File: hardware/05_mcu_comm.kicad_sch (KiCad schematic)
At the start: 0 parts

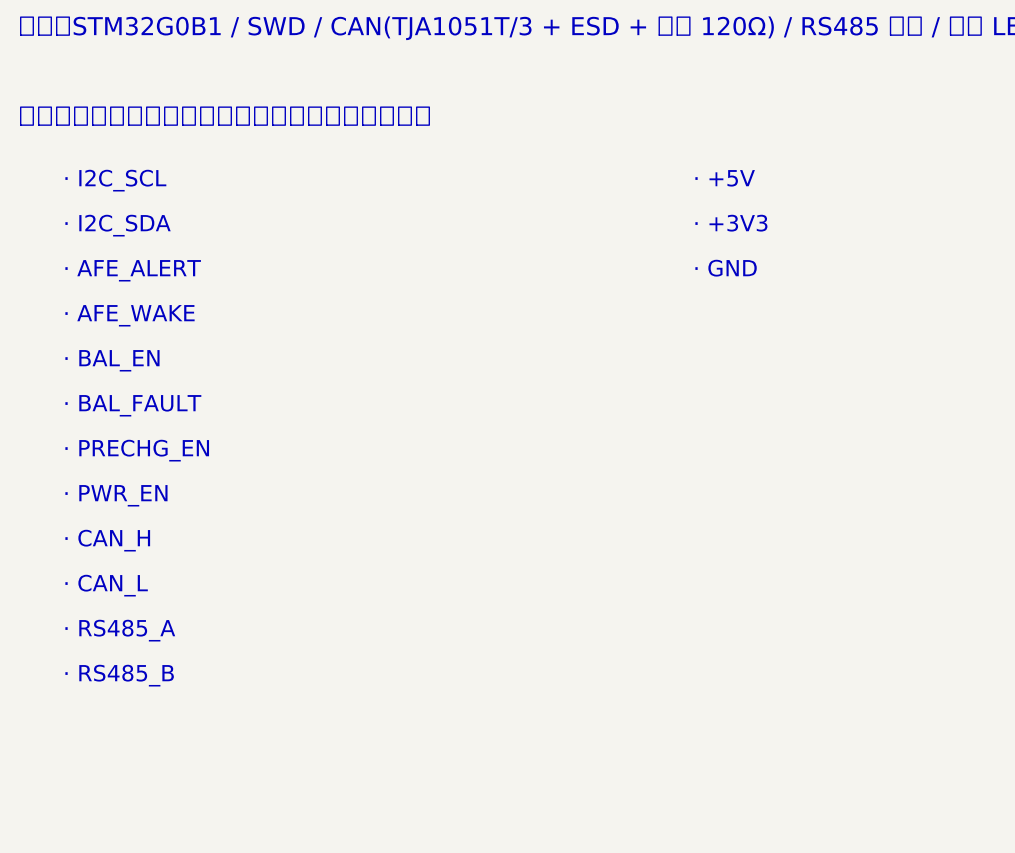
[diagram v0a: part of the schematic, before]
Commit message: v0.3：主动均衡改为 MP2643 ×7（MPS 客供），光耦跨电位控制，逐对均衡策略，BOM 与成本估算
- docs/03：均衡章节按 MP2643 手册 Rev1.1 重写（外围逐件点名、电流/限压计算、光耦接口、线束与发热）
- firmware：7 对 EN/MODE 输出，边界电荷盈亏定方向，相邻不同时开，收敛仿真测试
- tools/bms_calc.py：MP2643 手册公式；tools/jlc_api.py：嘉立创料号接口；tools/cost.py：成本估算
- docs/02-BOM.csv v0.3（81 行，带立创编号与来源），docs/05-成本估算.md
- KiCad 骨架更新（03 子图接口、网络类）

Co-Authored-By: Claude Opus 5.5 <noreply@anthropic.com>
Claude-Session: https://claude.ai/code/session_01EyFjq1nqLUmfVYESj2uYXd
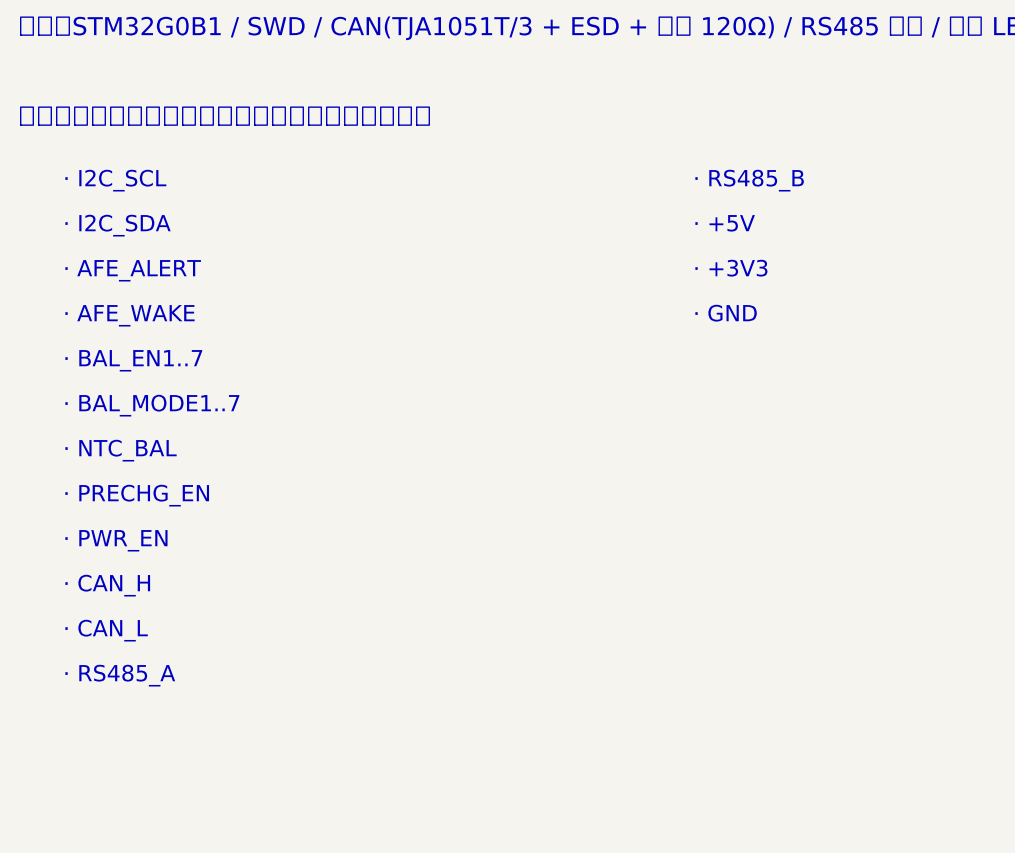
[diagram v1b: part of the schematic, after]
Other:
- note added: "· BAL_EN1..7"
- note added: "· BAL_MODE1..7"
- note added: "· NTC_BAL"
- note removed: "· BAL_EN"
- note removed: "· BAL_FAULT"
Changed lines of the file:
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@@
 		(title "MCU 与通讯")
 		(date "2026-09-26")
-		(rev "v0.2-skeleton")
+		(rev "v0.3-skeleton")
 		(company "MP2645A-BMS")
-		(comment 1 "8S LiFePO4 200A BMS · MPS MP2797 + MP2645A")
+		(comment 1 "8S LiFePO4 200A BMS · MPS MP2797 + MP2643x7")
 	)
 	(text "MCU 与通讯"
@@
 		)
 	)
-	(text "· BAL_EN"
+	(text "· BAL_EN1..7"
 		(exclude_from_sim no)
 		(at 25 72 0)
@@
 		)
 	)
-	(text "· BAL_FAULT"
+	(text "· BAL_MODE1..7"
 		(exclude_from_sim no)
 		(at 25 77 0)
@@
 		)
 	)
-	(text "· PRECHG_EN"
+	(text "· NTC_BAL"
 		(exclude_from_sim no)
 		(at 25 82 0)
@@
 		)
 	)
-	(text "· PWR_EN"
+	(text "· PRECHG_EN"
 		(exclude_from_sim no)
 		(at 25 87 0)
@@
 		)
 	)
-	(text "· CAN_H"
+	(text "· PWR_EN"
 		(exclude_from_sim no)
 		(at 25 92 0)
@@
 		)
 	)
-	(text "· CAN_L"
+	(text "· CAN_H"
 		(exclude_from_sim no)
 		(at 25 97 0)
@@
 		)
 	)
-	(text "· RS485_A"
+	(text "· CAN_L"
 		(exclude_from_sim no)
 		(at 25 102 0)
@@
 		)
 	)
-	(text "· RS485_B"
+	(text "· RS485_A"
 		(exclude_from_sim no)
 		(at 25 107 0)
@@
 		)
 	)
-	(text "· +5V"
+	(text "· RS485_B"
 		(exclude_from_sim no)
 		(at 95 52 0)
@@
 		)
 	)
-	(text "· +3V3"
+	(text "· +5V"
 		(exclude_from_sim no)
 		(at 95 57 0)
@@
 		)
 	)
-	(text "· GND"
+	(text "· +3V3"
 		(exclude_from_sim no)
 		(at 95 62 0)
 		(effects
 			(font
+				(size 1.8 1.8)
+			)
+			(justify left top)
+		)
+	)
+	(text "· GND"
+		(exclude_from_sim no)
+		(at 95 67 0)
+		(effects
+			(font

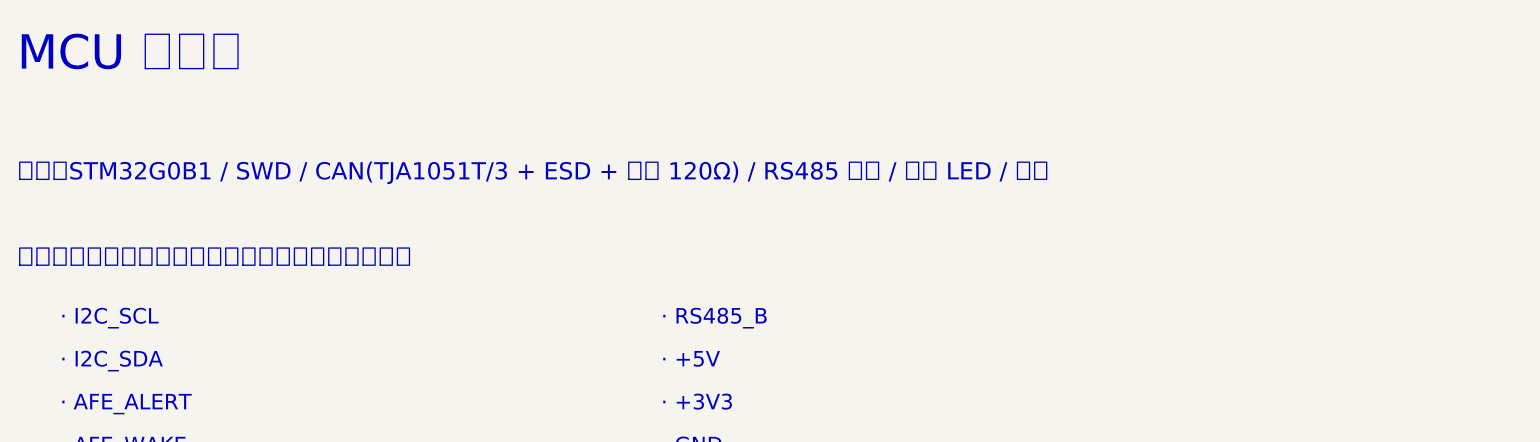
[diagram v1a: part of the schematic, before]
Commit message: v0.3 降本落地：Tokmas MOSFET×12、CH32V203、风华 4.7µF/100V、基础库阻值；MP2643 用 MPS 原厂 KiCad 库
- BOM：12 颗 Tokmas IPT012N08N5（C19626224）、CH32V203C8T6（C3001172）、C381466，MP2643 周边阻值改 0603 基础库等
- hardware/lib/mps：用户提供的 MP2643 符号/封装（已核对手册 p22 与引脚定义），注册到工程库表
- 计算器默认改为每方向 6 颗、Qg 240nC；测试按 Tj,max 150°C 留 30°C 裕量
- 成本：10 块 ¥587→¥393/块，100 块 ¥460→¥294/块（元器件）

Co-Authored-By: Claude Opus 5.5 <noreply@anthropic.com>
Claude-Session: https://claude.ai/code/session_01EyFjq1nqLUmfVYESj2uYXd
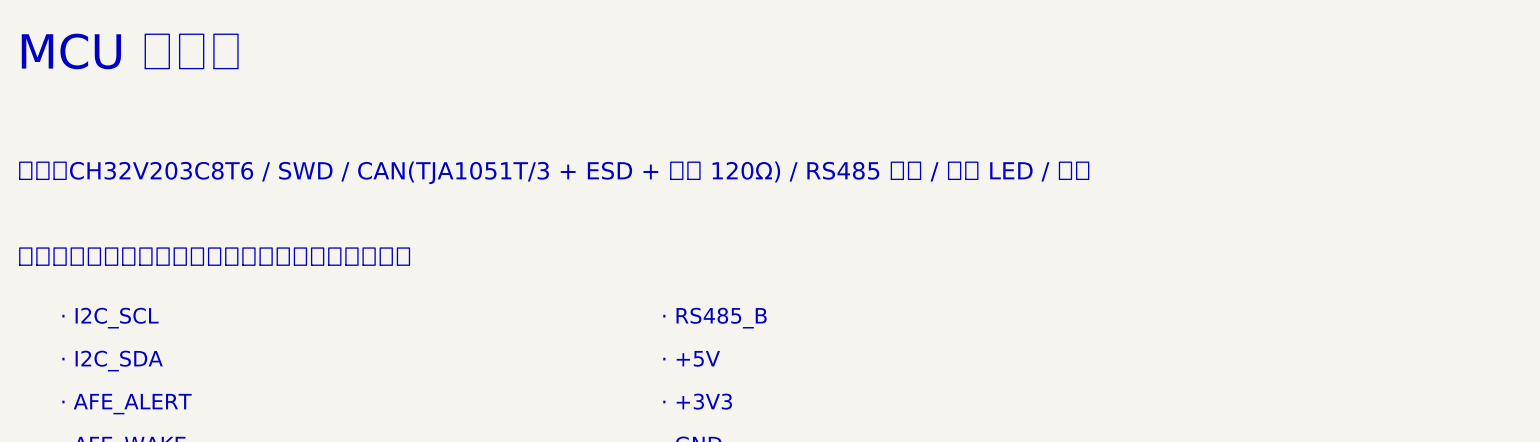
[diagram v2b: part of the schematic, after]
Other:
- note added: "内容：CH32V203C8T6 / SWD / CAN(TJA1051T/3 + ESD + 可选 120Ω) / RS485 可选 / 状态 LED / 按键"
- note removed: "内容：STM32G0B1 / SWD / CAN(TJA1051T/3 + ESD + 可选 120Ω) / RS485 可选 / 状态 LED / 按键"
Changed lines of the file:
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@@
 		)
 	)
-	(text "内容：STM32G0B1 / SWD / CAN(TJA1051T/3 + ESD + 可选 120Ω) / RS485 可选 / 状态 LED / 按键"
+	(text "内容：CH32V203C8T6 / SWD / CAN(TJA1051T/3 + ESD + 可选 120Ω) / RS485 可选 / 状态 LED / 按键"
 		(exclude_from_sim no)
 		(at 20 35 0)

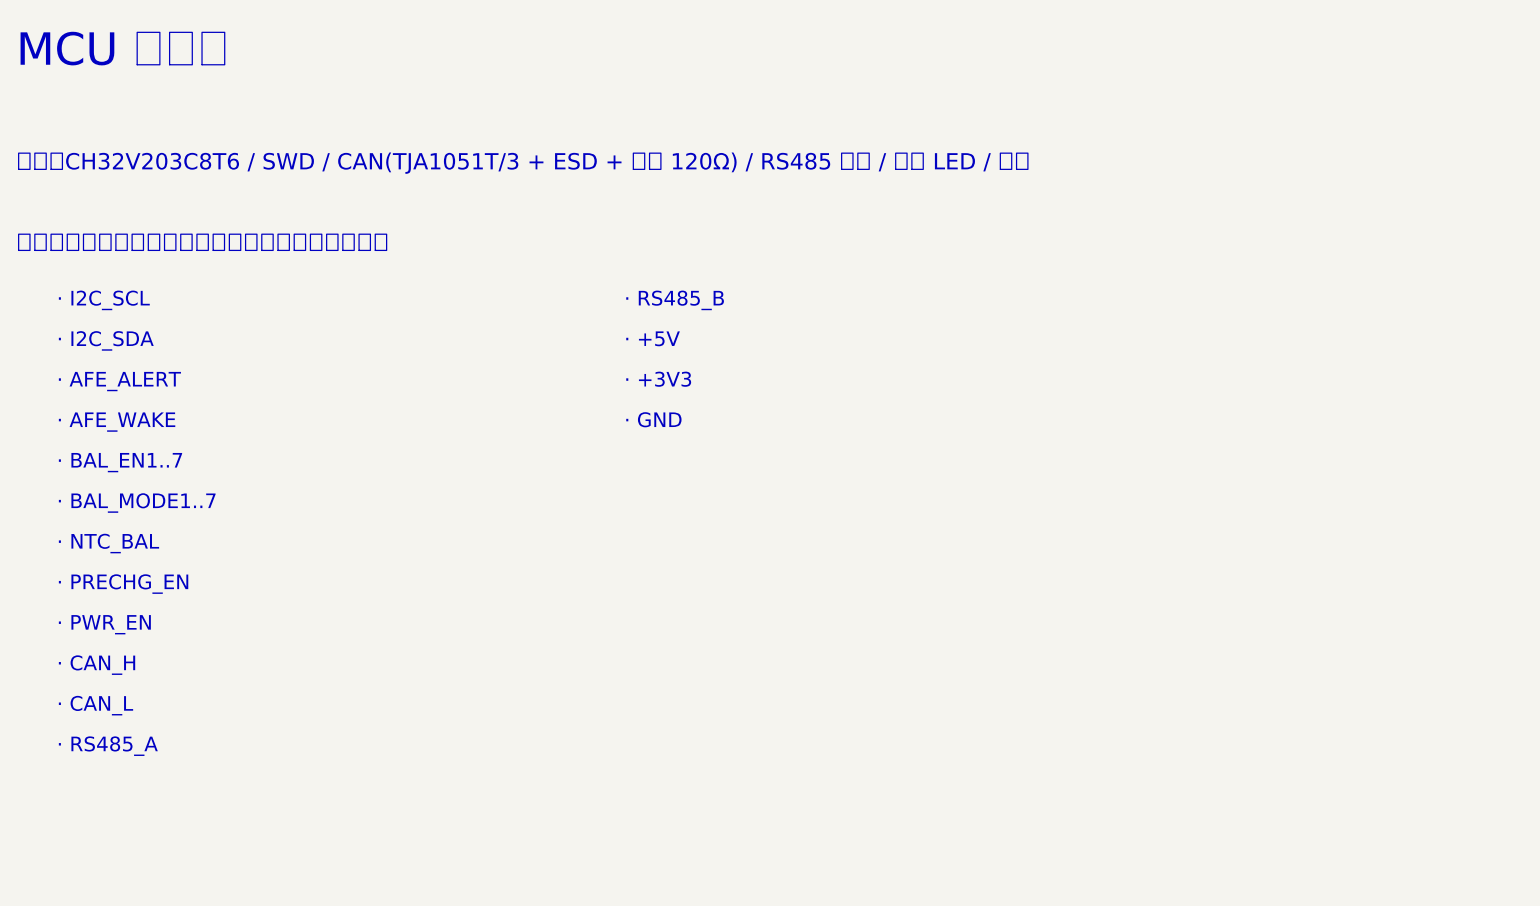
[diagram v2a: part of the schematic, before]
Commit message: 电源改为 LMR16006X 直降 3.3V + SN65HVD230（取消 5V 轨与 LDO）；会话交接文档与技能转移包
- BOM/详细设计/骨架：MP9486A+MP2013A+TJA1051 → LMR16006XDDCR(C87080)+SS210(C14996)+SN65HVD230DR(C12084)
- 成本（元器件）：10 块 ¥393→¥359/块，100 块 ¥294→¥267/块
- docs/00-会话交接.md：新会话的环境恢复、技能恢复、DeepSeek 画图方配置与待办
- transfer/pcb-workflow-skill.tar.gz：云主机上改写的 pcb-workflow 技能（仅用于转移）

Co-Authored-By: Claude Opus 5.5 <noreply@anthropic.com>
Claude-Session: https://claude.ai/code/session_01EyFjq1nqLUmfVYESj2uYXd
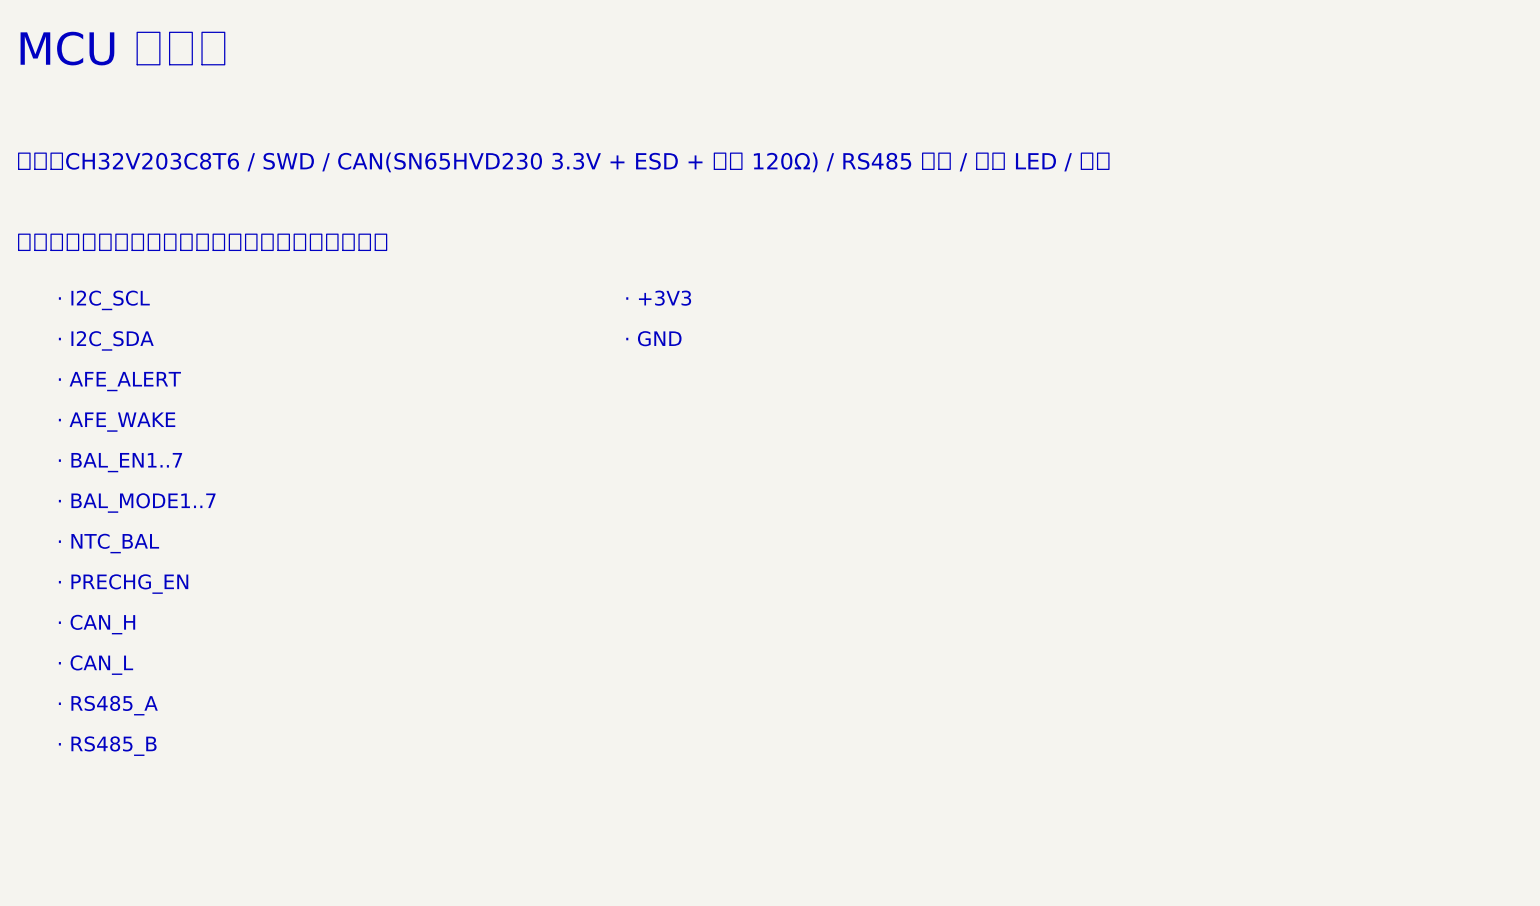
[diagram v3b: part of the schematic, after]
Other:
- note added: "内容：CH32V203C8T6 / SWD / CAN(SN65HVD230 3.3V + ESD + 可选 120Ω) / RS485 可选 / 状态 LED / 按键"
- note removed: "· +5V"
- note removed: "· PWR_EN"
- note removed: "内容：CH32V203C8T6 / SWD / CAN(TJA1051T/3 + ESD + 可选 120Ω) / RS485 可选 / 状态 LED / 按键"
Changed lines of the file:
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@@
 		)
 	)
-	(text "内容：CH32V203C8T6 / SWD / CAN(TJA1051T/3 + ESD + 可选 120Ω) / RS485 可选 / 状态 LED / 按键"
+	(text "内容：CH32V203C8T6 / SWD / CAN(SN65HVD230 3.3V + ESD + 可选 120Ω) / RS485 可选 / 状态 LED / 按键"
 		(exclude_from_sim no)
 		(at 20 35 0)
@@
 		)
 	)
-	(text "· PWR_EN"
+	(text "· CAN_H"
 		(exclude_from_sim no)
 		(at 25 92 0)
@@
 		)
 	)
-	(text "· CAN_H"
+	(text "· CAN_L"
 		(exclude_from_sim no)
 		(at 25 97 0)
@@
 		)
 	)
-	(text "· CAN_L"
+	(text "· RS485_A"
 		(exclude_from_sim no)
 		(at 25 102 0)
@@
 		)
 	)
-	(text "· RS485_A"
+	(text "· RS485_B"
 		(exclude_from_sim no)
 		(at 25 107 0)
@@
 		)
 	)
-	(text "· RS485_B"
+	(text "· +3V3"
 		(exclude_from_sim no)
 		(at 95 52 0)
@@
 		)
 	)
-	(text "· +5V"
+	(text "· GND"
 		(exclude_from_sim no)
 		(at 95 57 0)
 		(effects
 			(font
-				(size 1.8 1.8)
-			)
-			(justify left top)
-		)
-	)
-	(text "· +3V3"
-		(exclude_from_sim no)
-		(at 95 62 0)
-		(effects
-			(font
-				(size 1.8 1.8)
-			)
-			(justify left top)
-		)
-	)
-	(text "· GND"
-		(exclude_from_sim no)
-		(at 95 67 0)
-		(effects
-			(font

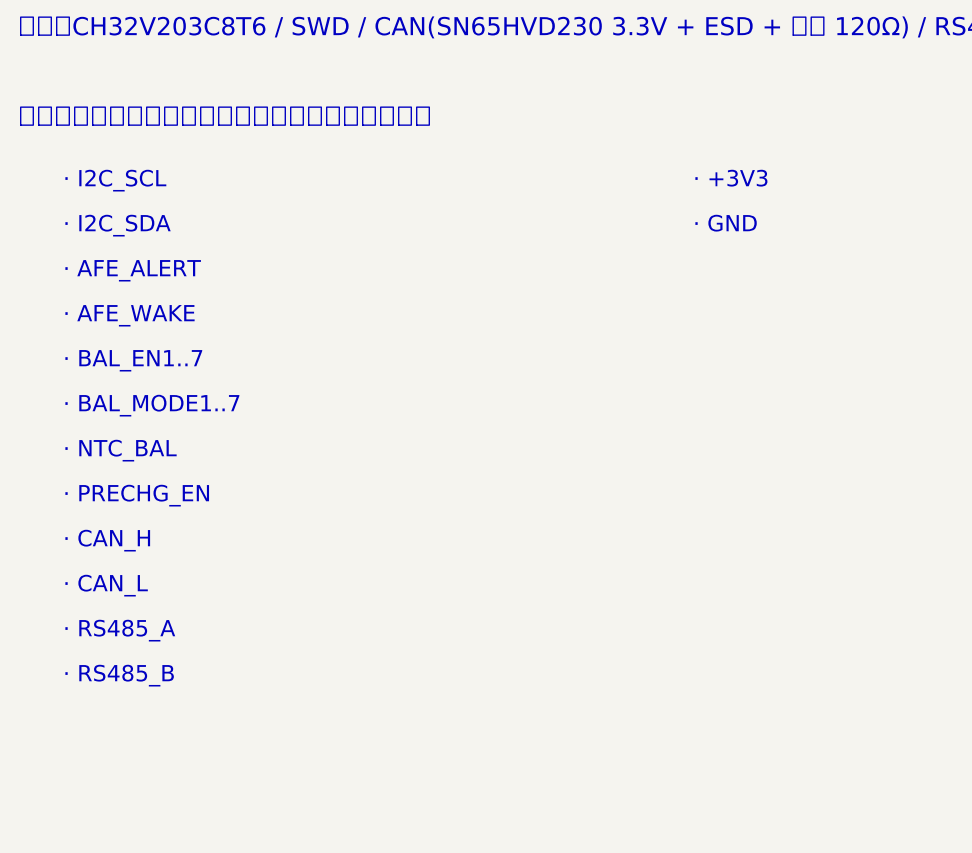
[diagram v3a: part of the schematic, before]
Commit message: 主动均衡改为分立开关电容（方案 B）：均衡部分约 ¥186→¥35/块
- 8 个互补半桥 AO3400A/AO3401A（基础库）+ 74LVC1G17 本节供电驱动，7 级飞电容 3×100µF，MCU BAL_CLK 50kHz 逐级电容耦合
- 固件：单一时钟使能；顶部/静置才开；压差>300mV 或任一节<3.0V 禁止；测试 37/37
- 计算器：sc_equalizer 模型（100mV≈0.21A，300mV≈0.62A）；测试 21/21
- BOM/成本：整板元器件 10 块 ¥359→¥202/块，100 块 ¥267→¥156/块
- 均衡端子改国产 2×5 Micro-Fit 兼容 C3030WV-2x5P（实测 3.0mm），节点保险丝 3A 1206

Co-Authored-By: Claude Opus 5.5 <noreply@anthropic.com>
Claude-Session: https://claude.ai/code/session_01EyFjq1nqLUmfVYESj2uYXd
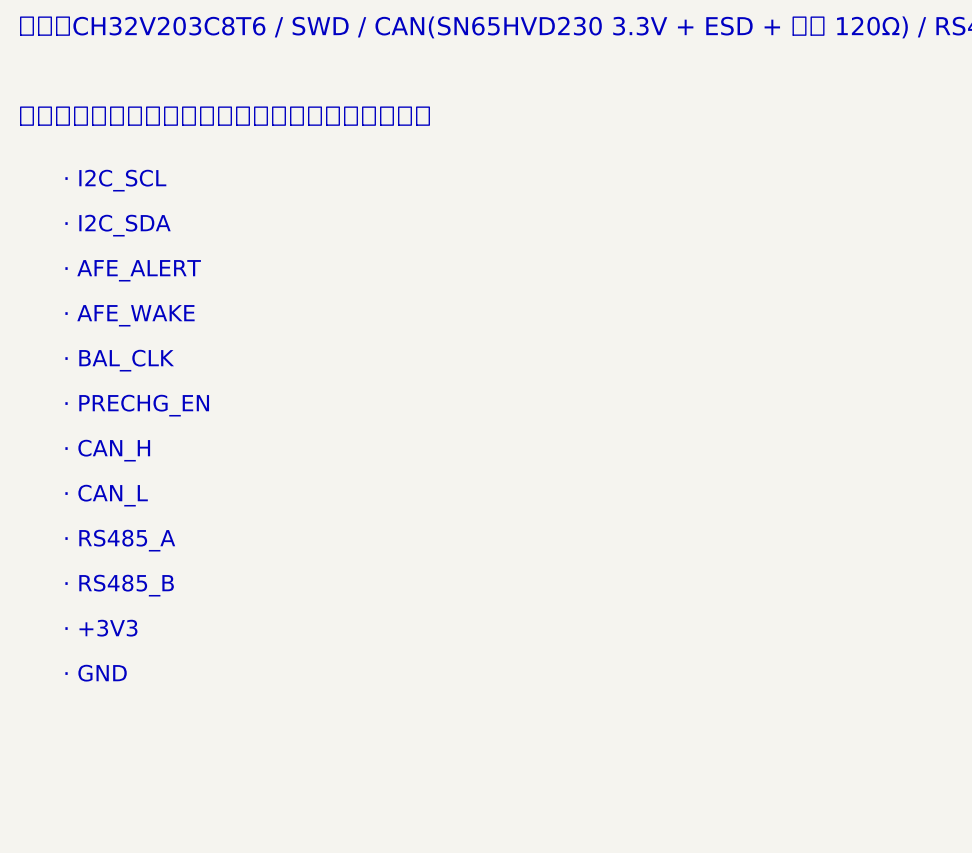
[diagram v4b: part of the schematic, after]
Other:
- note added: "· BAL_CLK"
- note removed: "· BAL_EN1..7"
- note removed: "· BAL_MODE1..7"
- note removed: "· NTC_BAL"
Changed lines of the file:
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@@
 		(rev "v0.3-skeleton")
 		(company "MP2645A-BMS")
-		(comment 1 "8S LiFePO4 200A BMS · MPS MP2797 + MP2643x7")
+		(comment 1 "8S LiFePO4 200A BMS · MPS MP2797 + 开关电容均衡")
 	)
 	(text "MCU 与通讯"
@@
 		)
 	)
-	(text "· BAL_EN1..7"
+	(text "· BAL_CLK"
 		(exclude_from_sim no)
 		(at 25 72 0)
@@
 		)
 	)
-	(text "· BAL_MODE1..7"
+	(text "· PRECHG_EN"
 		(exclude_from_sim no)
 		(at 25 77 0)
@@
 		)
 	)
-	(text "· NTC_BAL"
+	(text "· CAN_H"
 		(exclude_from_sim no)
 		(at 25 82 0)
@@
 		)
 	)
-	(text "· PRECHG_EN"
+	(text "· CAN_L"
 		(exclude_from_sim no)
 		(at 25 87 0)
@@
 		)
 	)
-	(text "· CAN_H"
+	(text "· RS485_A"
 		(exclude_from_sim no)
 		(at 25 92 0)
@@
 		)
 	)
-	(text "· CAN_L"
+	(text "· RS485_B"
 		(exclude_from_sim no)
 		(at 25 97 0)
@@
 		)
 	)
-	(text "· RS485_A"
+	(text "· +3V3"
 		(exclude_from_sim no)
 		(at 25 102 0)
@@
 		)
 	)
-	(text "· RS485_B"
+	(text "· GND"
 		(exclude_from_sim no)
 		(at 25 107 0)
 		(effects
 			(font
-				(size 1.8 1.8)
-			)
-			(justify left top)
-		)
-	)
-	(text "· +3V3"
-		(exclude_from_sim no)
-		(at 95 52 0)
-		(effects
-			(font
-				(size 1.8 1.8)
-			)
-			(justify left top)
-		)
-	)
-	(text "· GND"
-		(exclude_from_sim no)
-		(at 95 57 0)
-		(effects
-			(font
